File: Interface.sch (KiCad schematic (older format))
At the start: 22 parts, among them J301 IR LED, J302 Button, SW301 Reset, SW302 Push 1, SW303 Push 2, U301 ULN2003

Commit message: Little interface changing.
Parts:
- removed C301: 10u, Capacitors_SMD:C_0805, symbol C
- removed C302: 100n, Capacitors_SMD:C_0805, symbol C
- removed D301: LRTBG6TG, ledbox-newfootprints:LED-6-BIG, symbol LRTBG6TG
- removed J301: IR LED, Pin_Headers:Pin_Header_Straight_1x03, symbol Conn_01x03
- removed J302: Button, Pin_Headers:Pin_Header_Straight_1x02, symbol Conn_01x02
- removed R305, R311: 82, Resistors_SMD:R_0805, symbol R
- removed R306, R307: 22, Resistors_SMD:R_0805, symbol R
- removed R310: 10k, Resistors_SMD:R_0805, symbol R
- removed U301: ULN2003, Housings_SOIC:SOIC-16_3.9x9.9mm_Pitch1.27mm, symbol ULN2003
- added SW1: Push 3, Buttons_Switches_THT:SW_PUSH_6mm_h5mm, symbol SW_Push
- D302, D303: symbol LED -> LED-RESCUE-masterbox
- R304: value 150 -> 10k
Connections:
- net IR_LED_DRV is gone; now on net +5V: R304.1
- net GND: now also SW1.2
- net PUSH3: now reaches R304.2
- net PUSH3: now also SW1.1
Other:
- moved on the sheet: D302, D303, R308, R309

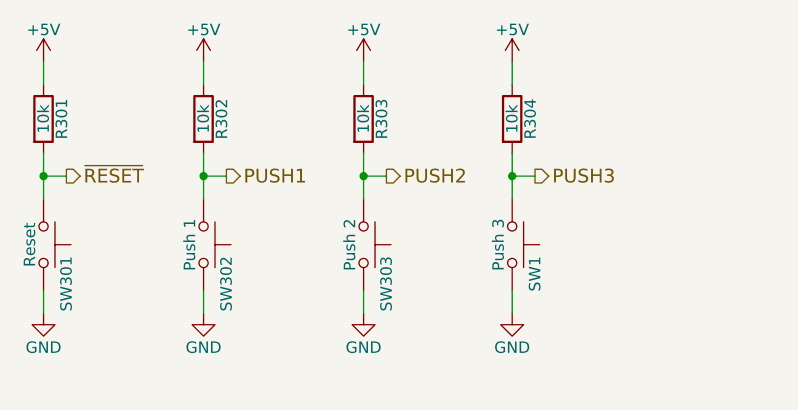
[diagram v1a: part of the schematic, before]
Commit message: ATmega2560 inserted
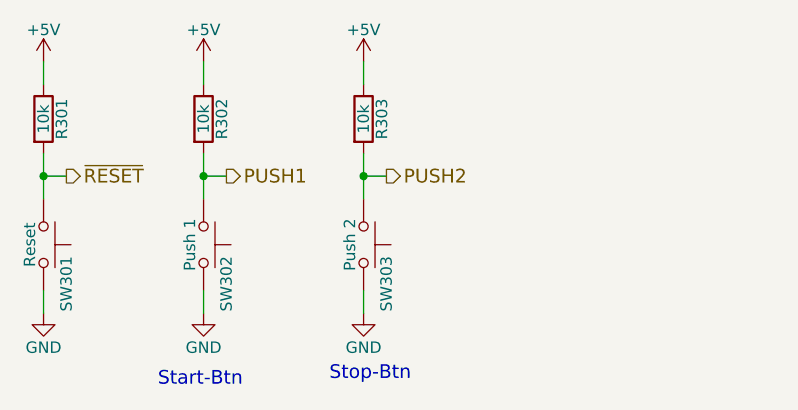
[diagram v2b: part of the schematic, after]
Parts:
- removed R304: 10k, Resistors_SMD:R_0805, symbol R
- removed SW1: Push 3, Buttons_Switches_THT:SW_PUSH_6mm_h5mm, symbol SW_Push
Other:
- note added: "Start-Btn\n"
- note added: "Stop-Btn"
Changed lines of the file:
@@
 Text HLabel 4300 5100 2    60   Output ~ 0
 PUSH1
-Text HLabel 5000 5100 2    60   Output ~ 0
-PUSH2
 Text HLabel 7950 5625 0    60   Input ~ 0
 LED1
@@
 Wire Wire Line
 	8750 5625 8750 5525
-$Comp
-L +5V #PWR026
-U 1 1 5A53FCDA
-P 5550 4600
-F 0 "#PWR026" H 5550 4450 50  0001 C CNN
-F 1 "+5V" H 5550 4740 50  0000 C CNN
-F 2 "" H 5550 4600 50  0001 C CNN
-F 3 "" H 5550 4600 50  0001 C CNN
-	1    5550 4600
-	1    0    0    -1
-$EndComp
-$Comp
-L R R304
-U 1 1 5A53FCE0
-P 5550 4850
-F 0 "R304" V 5630 4850 50  0000 C CNN
-F 1 "10k" V 5550 4850 50  0000 C CNN
-F 2 "Resistors_SMD:R_0805" V 5480 4850 50  0001 C CNN
-F 3 "" H 5550 4850 50  0001 C CNN
-	1    5550 4850
-	1    0    0    -1
-$EndComp
-Wire Wire Line
-	5550 5100 5650 5100
-Wire Wire Line
-	5550 5000 5550 5200
-Wire Wire Line
-	5550 4600 5550 4700
-$Comp
-L SW_Push SW1
-U 1 1 5A53FCE9
-P 5550 5400
-F 0 "SW1" H 5600 5500 50  0000 L CNN
-F 1 "Push 3" H 5550 5340 50  0000 C CNN
-F 2 "Buttons_Switches_THT:SW_PUSH_6mm_h5mm" H 5550 5600 50  0001 C CNN
-F 3 "" H 5550 5600 50  0001 C CNN
-	1    5550 5400
-	0    1    1    0
-$EndComp
-$Comp
-L GND #PWR027
-U 1 1 5A53FCEF
-P 5550 5700
-F 0 "#PWR027" H 5550 5450 50  0001 C CNN
-F 1 "GND" H 5550 5550 50  0000 C CNN
-F 2 "" H 5550 5700 50  0001 C CNN
-F 3 "" H 5550 5700 50  0001 C CNN
-	1    5550 5700
-	1    0    0    -1
-$EndComp
-Wire Wire Line
-	5550 5700 5550 5600
-Connection ~ 5550 5100
-Text HLabel 5650 5100 2    60   Output ~ 0
-PUSH3
+Text HLabel 5000 5100 2    60   Output ~ 0
+PUSH2
+Text Notes 4000 6025 0    60   ~ 0
+Start-Btn\n
+Text Notes 4750 6000 0    60   ~ 0
+Stop-Btn
 $EndSCHEMATC
